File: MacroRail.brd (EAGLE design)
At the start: 42.9 x 81.5 mm, 23 parts, among them CN2 1X4-3.5MM, CN3 SJ1-2503A, Q1 TIP120, U1 ESP32DEVKITC, U2 TMC2209-V1.2+INDEX

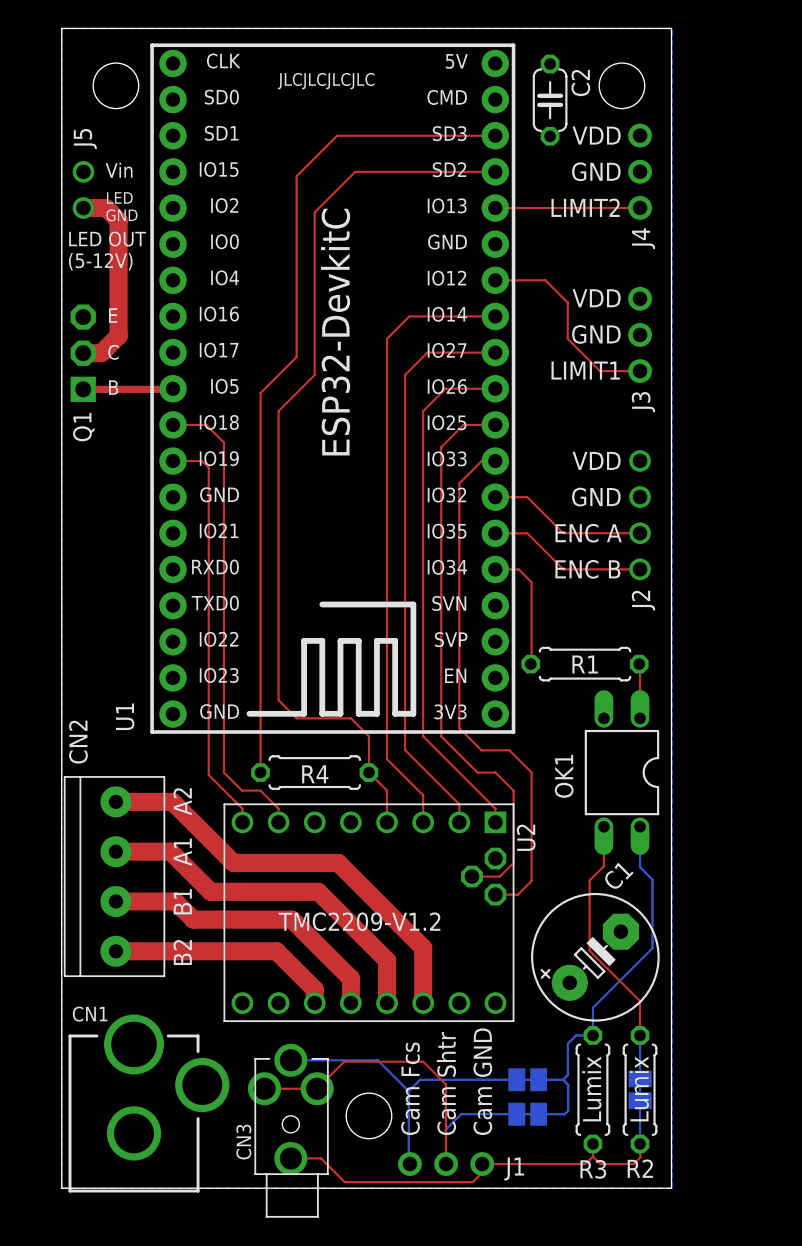
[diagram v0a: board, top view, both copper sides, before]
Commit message: V1 Revision 1
Large redesign of the board. Made board wider (50x80mm now). Moved connections to make them more accessible when PCB is mounted on macro slider. Added transistor for driving LED illumination. Added more connections to TMC driver (UART and Index). Added capacitance to EN pin after noticing this helps with automatic bootloader entry during programming.
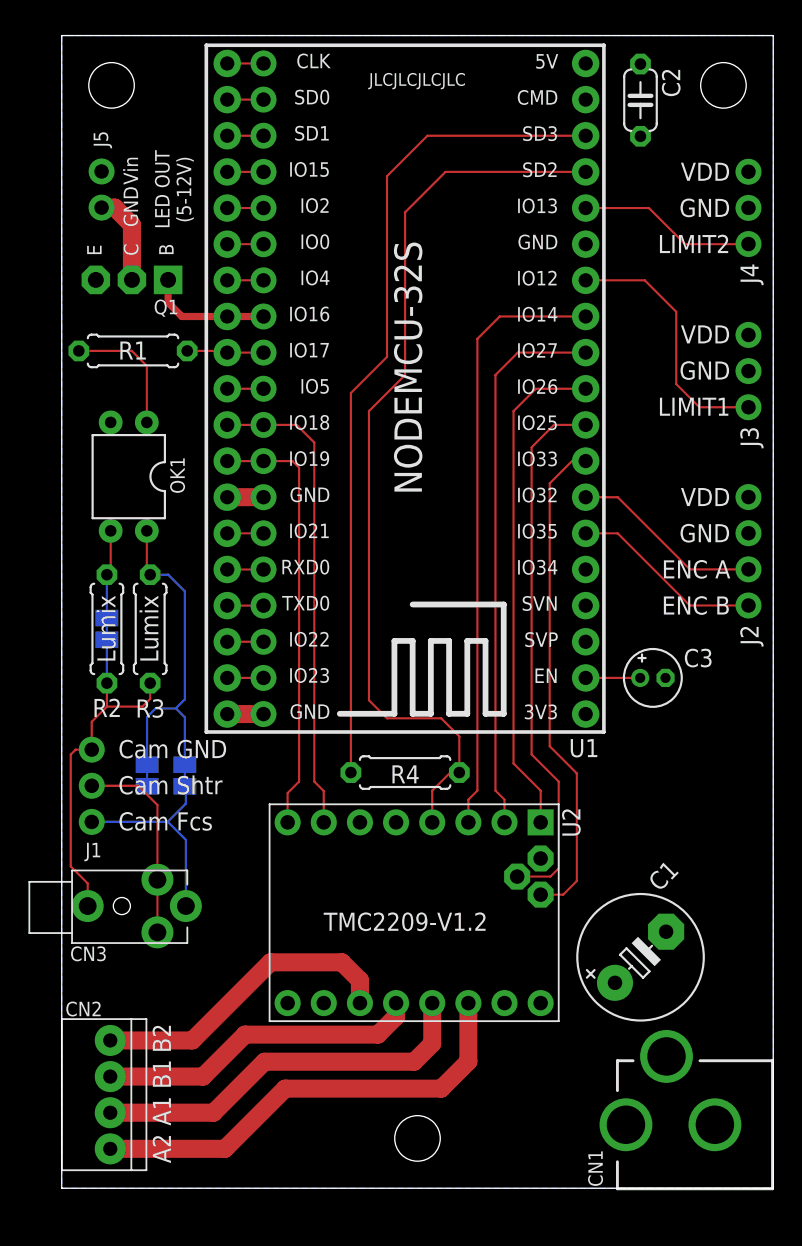
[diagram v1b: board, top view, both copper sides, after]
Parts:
- added C3: 10uF, rcl:E1,8-4
- added JP1: (no value), pinhead-custom:1X19
- CN1: device adafruit:DCJACK_2MM_PTH -> 00-Random-Components-Simen:DCJACK_2MM_PTH
- CN2: value 1X4-3.5MM -> 1X4-2.54MM; device adafruit:1X04-3.5MM -> 00-Random-Components-Simen:1X04-2.54MM
- OK1: device optocoupler:DIL04 -> 00-Random-Components-Simen:DIL04
- U1: value ESP32DEVKITC -> ESP32DEVKITCWIDE; device ESP32-DEVKITC:ESP32-DEVKITC -> ESP32-DEVKITC:NODEMCU-32S
- moved R2 49.5 mm to (3.17, 39.3)
- moved SJ1 49.5 mm to (3.17, 39.3)
- moved CN1 48.8 mm to (53.2, 4.46), turned to 90 degrees
- moved R3 44.9 mm to (6.21, 39.3)
- moved OK1 40.4 mm to (4.71, 50.0)
- moved R1 38.6 mm to (5.01, 58.8), turned to 0 degrees
- moved J1 36.4 mm to (2.11, 28.3), turned to 90 degrees
- moved SJ3 35.8 mm to (6.00, 29.0), turned to 90 degrees
- moved SJ2 32.2 mm to (8.65, 29.0), turned to 270 degrees
- moved U$3 20.8 mm to (24.6, 35.4)
- moved CN3 19.4 mm to (4.22, 19.8), turned to 0 degrees
- moved CN2 15.3 mm to (3.41, 6.58)
- moved Q1 9.73 mm to (7.47, 63.8), turned to 180 degrees
- moved J4 8.03 mm to (48.3, 68.9)
- moved J2 8.03 mm to (48.3, 44.8)
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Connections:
- new net N$10: JP1.6, U1.25
- new net N$11: JP1.5, U1.24
- new net N$12: JP1.4, U1.23
- new net N$13: JP1.3, U1.22
- new net N$14: JP1.2, U1.21
- new net N$15: JP1.1, U1.20
- new net N$2: C3.+, U1.2
- new net N$3: JP1.18, U1.37
- new net N$4: JP1.17, U1.36
- new net N$5: JP1.16, U1.35
- new net N$6: JP1.15, U1.34
- new net N$7: JP1.14, U1.33
- new net N$8: JP1.10, U1.29
- new net N$9: JP1.7, U1.26
- net A1: now also CN2.3; no longer CN2.2
- net A2: now also CN2.4; no longer CN2.1
- net B1: now also CN2.2; no longer CN2.3
- net B2: now also CN2.1; no longer CN2.4
- net GND: now also C3.-, JP1.13, JP1.19
- net LED_PWM: now also JP1.8, U1.27; no longer U1.29
- net SHUTTER: now also JP1.9, U1.28; no longer U1.5
- net STEP: now also JP1.11
- net STEP_DIR: now also JP1.12
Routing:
- net CAM_FOCUS_SHUTTER: track 80.6 -> 60.4 mm
- net CAM_GND: track 52.8 -> 33.1 mm
- net LED_GND: track 13.9 -> 6.51 mm
- net B2: track 16.0 -> 21.9 mm
- net N$1: track 3.83 -> 9.19 mm
- net GND: track 0.00 -> 5.10 mm
- net N$2: track 0.00 -> 3.83 mm
- net LIMIT1: track 14.3 -> 18.1 mm
- net SHUTTER: track 8.70 -> 5.41 mm
- net N$9: track 0.00 -> 2.55 mm
- net N$8: track 0.00 -> 2.55 mm
- net N$7: track 0.00 -> 2.55 mm
- net N$6: track 0.00 -> 2.55 mm
- net N$5: track 0.00 -> 2.55 mm
- net N$4: track 0.00 -> 2.55 mm
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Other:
- board size 42.9 x 81.5 mm -> 50 x 81 mm
- board text added: "Design by: Simen E. Sørensen"
- board text removed: "Simen E. Sørensen"

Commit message: Move TMC UART communication to Serial2
Serial1 is already occupied by the ESP flash, so we need to use Serial2 instead. This interface was already in use by the SHUTTER- and LED_PWM-signals, so they had to be moved as well.
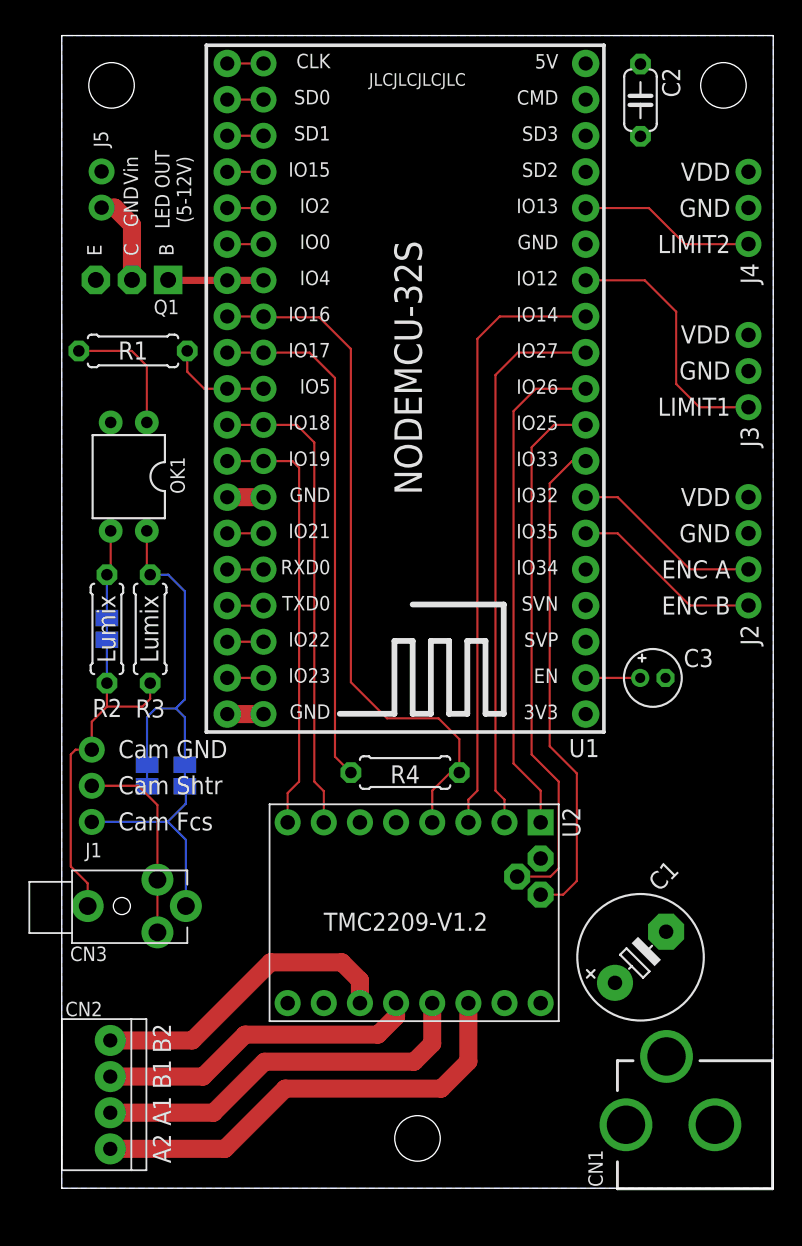
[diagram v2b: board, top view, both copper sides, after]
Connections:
- removed net N$8: JP1.10, U1.29
- removed net N$9: JP1.7, U1.26
- new net U2RXD: JP1.8, R4.1, U1.27, U2.PDN_1
- new net U2TXD: JP1.9, R4.2, U1.28
- net LED_PWM: now also JP1.7, U1.26; no longer JP1.8, U1.27
- net SHUTTER: now also JP1.10, U1.29; no longer JP1.9, U1.28
- net U1RXD: no longer R4.1, U2.PDN_1
- net U1TXD: no longer R4.2
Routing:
- net U1RXD: track 63.8 -> 0.00 mm
- net U1TXD: track 58.1 -> 0.00 mm
- net U2RXD: track 0.00 -> 49.3 mm
- net U2TXD: track 0.00 -> 36.5 mm
- net N$9: track 2.55 -> 0.00 mm
- net N$8: track 2.55 -> 0.00 mm
- net LED_PWM: track 8.71 -> 6.72 mm
- net SHUTTER: track 5.41 -> 7.32 mm
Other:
- board text added: "Motorized Macro Slider V1.2"
- board text removed: "Motorized Macro Slider V1.1"
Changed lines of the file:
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@@
 <text x="5.055" y="17.98" size="0.8128" layer="26" rot="MR90" align="top-center">TIP</text>
 <text x="10.235" y="19.83" size="0.8128" layer="26" rot="MR90" align="bottom-center">RING</text>
-<text x="17.78" y="80.01" size="1.778" layer="26" rot="SMR270">Motorized Macro Slider V1.1</text>
+<text x="17.78" y="80.01" size="1.778" layer="26" rot="SMR270">Motorized Macro Slider V1.2</text>
 <text x="20.32" y="80.01" size="1.778" layer="26" rot="SMR270">Docs: GitHub.com/AppliedProcrastination</text>
 <text x="36.195" y="15.24" size="1.016" layer="26" rot="MR0">User must verify shutter-circuit
@@
 <signal name="SHUTTER">
 <contactref element="R1" pad="2"/>
-<contactref element="U1" pad="28"/>
-<wire x1="11.63" y1="58.72" x2="11.51" y2="58.84" width="0.1524" layer="1"/>
-<wire x1="11.51" y1="58.84" x2="8.82" y2="58.84" width="0.1524" layer="1"/>
-<contactref element="JP1" pad="9"/>
-<wire x1="14.18" y1="58.72" x2="11.63" y2="58.72" width="0.1524" layer="1"/>
+<contactref element="JP1" pad="10"/>
+<contactref element="U1" pad="29"/>
+<wire x1="11.63" y1="56.18" x2="14.18" y2="56.18" width="0.1524" layer="1"/>
+<wire x1="11.63" y1="56.18" x2="10.02" y2="56.18" width="0.1524" layer="1"/>
+<wire x1="8.82" y1="57.38" x2="8.82" y2="58.84" width="0.1524" layer="1"/>
+<wire x1="10.02" y1="56.18" x2="8.82" y2="57.38" width="0.1524" layer="1"/>
 </signal>
 <signal name="LIMIT1">
@@
 </signal>
 <signal name="U1TXD">
-<contactref element="R4" pad="2"/>
 <contactref element="U1" pad="17"/>
-<wire x1="36.82" y1="73.96" x2="25.7" y2="73.96" width="0.1524" layer="1"/>
-<wire x1="22.86" y1="71.12" x2="22.86" y2="58.42" width="0.1524" layer="1"/>
-<wire x1="22.86" y1="58.42" x2="20.32" y2="55.88" width="0.1524" layer="1"/>
-<wire x1="20.32" y1="55.88" x2="20.32" y2="29.21" width="0.1524" layer="1"/>
-<wire x1="25.7" y1="73.96" x2="22.86" y2="71.12" width="0.1524" layer="1"/>
 </signal>
 <signal name="U1RXD">
-<contactref element="R4" pad="1"/>
 <contactref element="U1" pad="16"/>
-<wire x1="27.94" y1="29.21" x2="27.94" y2="31.75" width="0.1524" layer="1"/>
-<wire x1="27.94" y1="31.75" x2="26.67" y2="33.02" width="0.1524" layer="1"/>
-<wire x1="26.67" y1="33.02" x2="22.86" y2="33.02" width="0.1524" layer="1"/>
-<wire x1="22.86" y1="33.02" x2="21.59" y2="34.29" width="0.1524" layer="1"/>
-<wire x1="21.59" y1="54.61" x2="24.13" y2="57.15" width="0.1524" layer="1"/>
-<wire x1="24.13" y1="57.15" x2="24.13" y2="68.58" width="0.1524" layer="1"/>
-<wire x1="24.13" y1="68.58" x2="26.97" y2="71.42" width="0.1524" layer="1"/>
-<wire x1="26.97" y1="71.42" x2="36.82" y2="71.42" width="0.1524" layer="1"/>
-<wire x1="21.59" y1="34.29" x2="21.59" y2="54.61" width="0.1524" layer="1"/>
-<wire x1="27.94" y1="29.21" x2="27.305" y2="29.21" width="0.1524" layer="1"/>
-<wire x1="27.305" y1="29.21" x2="26.035" y2="27.94" width="0.1524" layer="1"/>
-<wire x1="26.035" y1="27.94" x2="26.035" y2="25.71" width="0.1524" layer="1"/>
-<contactref element="U2" pad="PDN_1"/>
 </signal>
 <signal name="STEP_DIAG">
@@
 <signal name="LED_PWM">
 <contactref element="Q1" pad="B"/>
-<wire x1="7.475" y1="62.23" x2="7.475" y2="63.83" width="0.508" layer="1"/>
-<contactref element="U1" pad="27"/>
-<wire x1="11.63" y1="61.26" x2="8.445" y2="61.26" width="0.508" layer="1"/>
-<wire x1="8.445" y1="61.26" x2="7.475" y2="62.23" width="0.508" layer="1"/>
-<contactref element="JP1" pad="8"/>
-<wire x1="11.63" y1="61.26" x2="14.18" y2="61.26" width="0.508" layer="1"/>
+<contactref element="U1" pad="26"/>
+<contactref element="JP1" pad="7"/>
+<wire x1="11.63" y1="63.8" x2="7.505" y2="63.8" width="0.508" layer="1"/>
+<wire x1="7.505" y1="63.8" x2="7.475" y2="63.83" width="0.508" layer="1"/>
+<wire x1="14.18" y1="63.8" x2="11.63" y2="63.8" width="0.508" layer="1"/>
 </signal>
 <signal name="LED_GND">
@@
 <wire x1="11.63" y1="46.02" x2="14.18" y2="46.02" width="0.1524" layer="1"/>
 </signal>
-<signal name="N$8">
-<contactref element="JP1" pad="10"/>
-<contactref element="U1" pad="29"/>
-<wire x1="11.63" y1="56.18" x2="14.18" y2="56.18" width="0.1524" layer="1"/>
-</signal>
-<signal name="N$9">
-<contactref element="U1" pad="26"/>
-<contactref element="JP1" pad="7"/>
-<wire x1="14.18" y1="63.8" x2="11.63" y2="63.8" width="0.1524" layer="1"/>
-</signal>
 <signal name="N$10">
 <contactref element="JP1" pad="6"/>
@@
 <wire x1="14.18" y1="79.04" x2="11.63" y2="79.04" width="0.1524" layer="1"/>
 </signal>
+<signal name="U2TXD">
+<contactref element="U1" pad="28"/>
+<contactref element="JP1" pad="9"/>
+<wire x1="14.18" y1="58.72" x2="11.63" y2="58.72" width="0.1524" layer="1"/>
+<contactref element="R4" pad="2"/>
+<wire x1="14.18" y1="58.72" x2="17.42" y2="58.72" width="0.1524" layer="1"/>
+<wire x1="19.2" y1="30.33" x2="20.32" y2="29.21" width="0.1524" layer="1"/>
+<wire x1="17.42" y1="58.72" x2="19.2" y2="56.94" width="0.1524" layer="1"/>
+<wire x1="19.2" y1="56.94" x2="19.2" y2="30.33" width="0.1524" layer="1"/>
+</signal>
+<signal name="U2RXD">
+<contactref element="U1" pad="27"/>
+<contactref element="JP1" pad="8"/>
+<contactref element="R4" pad="1"/>
+<contactref element="U2" pad="PDN_1"/>
+<wire x1="27.94" y1="29.21" x2="27.305" y2="29.21" width="0.1524" layer="1"/>
+<wire x1="27.305" y1="29.21" x2="26.035" y2="27.94" width="0.1524" layer="1"/>
+<wire x1="26.035" y1="27.94" x2="26.035" y2="25.71" width="0.1524" layer="1"/>
+<wire x1="11.63" y1="61.26" x2="14.18" y2="61.26" width="0.1524" layer="1"/>
+<wire x1="14.18" y1="61.26" x2="14.24" y2="61.2" width="0.1524" layer="1"/>
+<wire x1="14.24" y1="61.2" x2="18.1" y2="61.2" width="0.1524" layer="1"/>
+<wire x1="18.1" y1="61.2" x2="20.32" y2="58.98" width="0.1524" layer="1"/>
+<wire x1="20.32" y1="35.56" x2="22.86" y2="33.02" width="0.1524" layer="1"/>
+<wire x1="27.94" y1="31.56" x2="27.94" y2="29.21" width="0.1524" layer="1"/>
+<wire x1="20.32" y1="58.98" x2="20.32" y2="35.56" width="0.1524" layer="1"/>
+<wire x1="22.86" y1="33.02" x2="26.48" y2="33.02" width="0.1524" layer="1"/>
+<wire x1="26.48" y1="33.02" x2="27.94" y2="31.56" width="0.1524" layer="1"/>
+</signal>
 </signals>

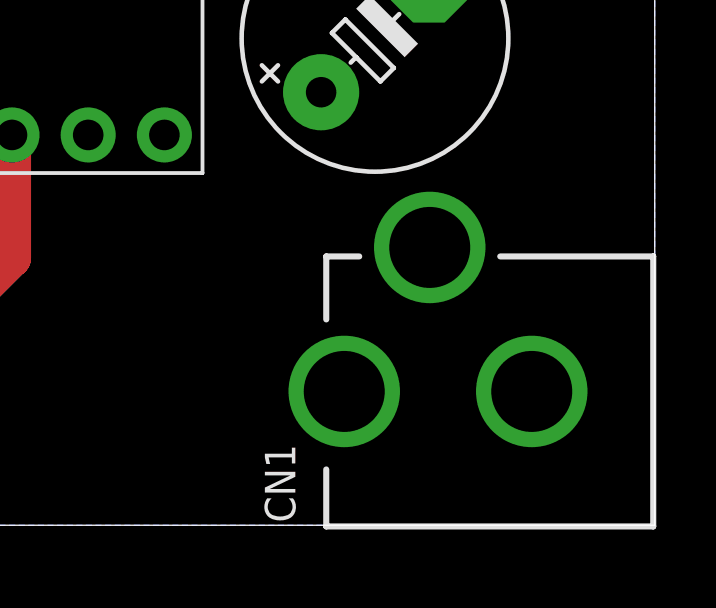
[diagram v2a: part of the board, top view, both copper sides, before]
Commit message: Update documentation to match V1.2
V1.2 is the first fully functional design
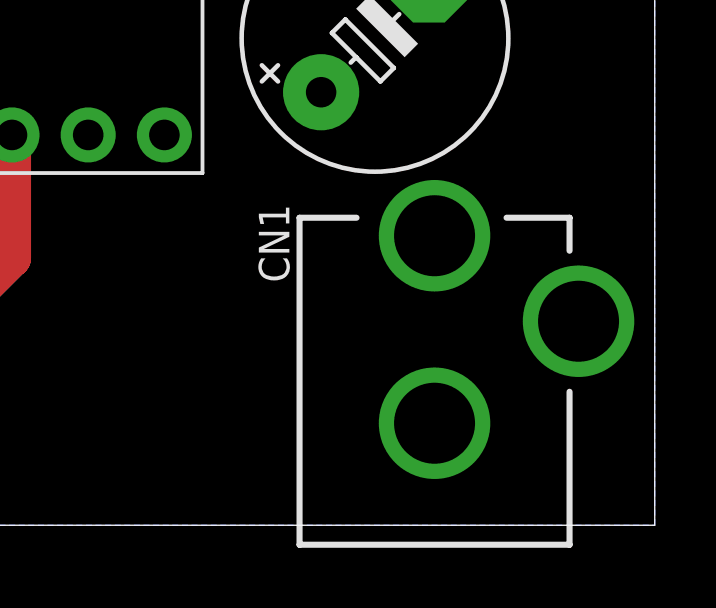
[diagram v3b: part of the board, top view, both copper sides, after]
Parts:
- moved CN1 13.5 mm to (42.7, -3.95), turned to 0 degrees
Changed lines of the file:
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@@
 </layers>
 <board>
-<fusionsync huburn="a.cGVyc29uYWw6dWUyYjkwZjE2" projecturn="a.cGVyc29uYWw6dWUyYjkwZjE2IzIwMTgwOTA0MTQ2OTc5MDgx" f3durn="urn:adsk.wipprod:dm.lineage:p6BxFAy9R-OurxXYLrTLuw" pcbguid="dc448735-d099-4600-9fa7-d1462ebbee2b" lastpulledtime="" lastsyncedchangeguid="c9a359a8-8276-b33f-54dc-8abe83486807"/>
+<fusionsync huburn="a.cGVyc29uYWw6dWUyYjkwZjE2" projecturn="a.cGVyc29uYWw6dWUyYjkwZjE2IzIwMTgwOTA0MTQ2OTc5MDgx" f3durn="urn:adsk.wipprod:dm.lineage:p6BxFAy9R-OurxXYLrTLuw" pcbguid="dc448735-d099-4600-9fa7-d1462ebbee2b" lastpulledtime="" lastsyncedchangeguid="b1865a2a-e328-c488-8da2-12f6c6c320b7"/>
 <plain>
 <wire x1="0" y1="0" x2="50" y2="0" width="0" layer="20"/>
@@
 <hole x="46.5" y="77.5" drill="3.2"/>
 <hole x="3.5" y="77.5" drill="3.2"/>
-<text x="36.765" y="4.41" size="0.889" layer="26" rot="SMR0" align="center-left">Vin (5-12V)</text>
-<text x="39.75" y="9.06" size="0.889" layer="26" rot="SMR0">GND</text>
+<text x="39.665" y="9.61" size="0.889" layer="26" rot="SMR0" align="center-left">Vin (5-12V)</text>
+<text x="39.665" y="3.46" size="0.889" layer="26" rot="SMR0" align="center-left">GND</text>
 <text x="21.59" y="77.47" size="0.889" layer="25">JLCJLCJLCJLC</text>
 <text x="6.155" y="39.305" size="1.27" layer="25" rot="R90" align="center">Lumix</text>
@@
 <attribute name="VALUE" x="5.285" y="24.47" size="1.27" layer="27" rot="R90"/>
 </element>
-<element name="CN1" library="00-Random-Components-Simen" library_urn="urn:adsk.eagle:library:24319138" package="DCJACK_2MM_PTH" package3d_urn="urn:adsk.eagle:package:34759908/1" override_package3d_urn="urn:adsk.eagle:package:34287631/2" override_package_urn="urn:adsk.eagle:footprint:6240083/1" override_locally_modified="yes" value="" x="53.25" y="4.46" smashed="yes" rot="R90">
-<attribute name="NAME" x="38.02" y="0.09" size="1.016" layer="25" rot="R90"/>
-<attribute name="VALUE" x="53.25" y="10.81" size="1.27" layer="27" rot="R180"/>
+<element name="CN1" library="00-Random-Components-Simen" library_urn="urn:adsk.eagle:library:24319138" package="DCJACK_2MM_PTH" package3d_urn="urn:adsk.eagle:package:34759908/1" override_package3d_urn="urn:adsk.eagle:package:34287631/2" override_package_urn="urn:adsk.eagle:footprint:6240083/1" override_locally_modified="yes" value="" x="42.66" y="-3.95" smashed="yes">
+<attribute name="NAME" x="37.82" y="8.09" size="1.016" layer="25" rot="R90"/>
+<attribute name="VALUE" x="49.01" y="-3.95" size="1.27" layer="27" rot="R90"/>
 </element>
 <element name="J3" library="adafruit" library_urn="urn:adsk.eagle:library:420" package="1X03-CLEANBIG" package3d_urn="urn:adsk.eagle:package:6240706/1" override_package3d_urn="urn:adsk.eagle:package:34287821/2" override_package_urn="urn:adsk.eagle:footprint:6240060/1" value="" x="48.26" y="57.4219" smashed="yes" rot="R90">
